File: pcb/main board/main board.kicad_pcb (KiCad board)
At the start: 2 copper layers, 115 x 160.5 mm, 75 parts, among them J1 Motor 0 Conn, J10 12V Battery, J11 BAU, J12 Servo 4 Conn, J13 Servo 1 Conn, J14 Servo 2 Conn, J15 Servo 3 Conn, J16 Servo 5 Conn, J17 Servo 6 Conn, J18 Servo 7 Conn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

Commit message: Added logos and aisler logo placeholder
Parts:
- added G***: LOGO, LOGO, F.Cu at (247.0, 101.0)
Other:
- board text added: "Made by Piment Robotique"

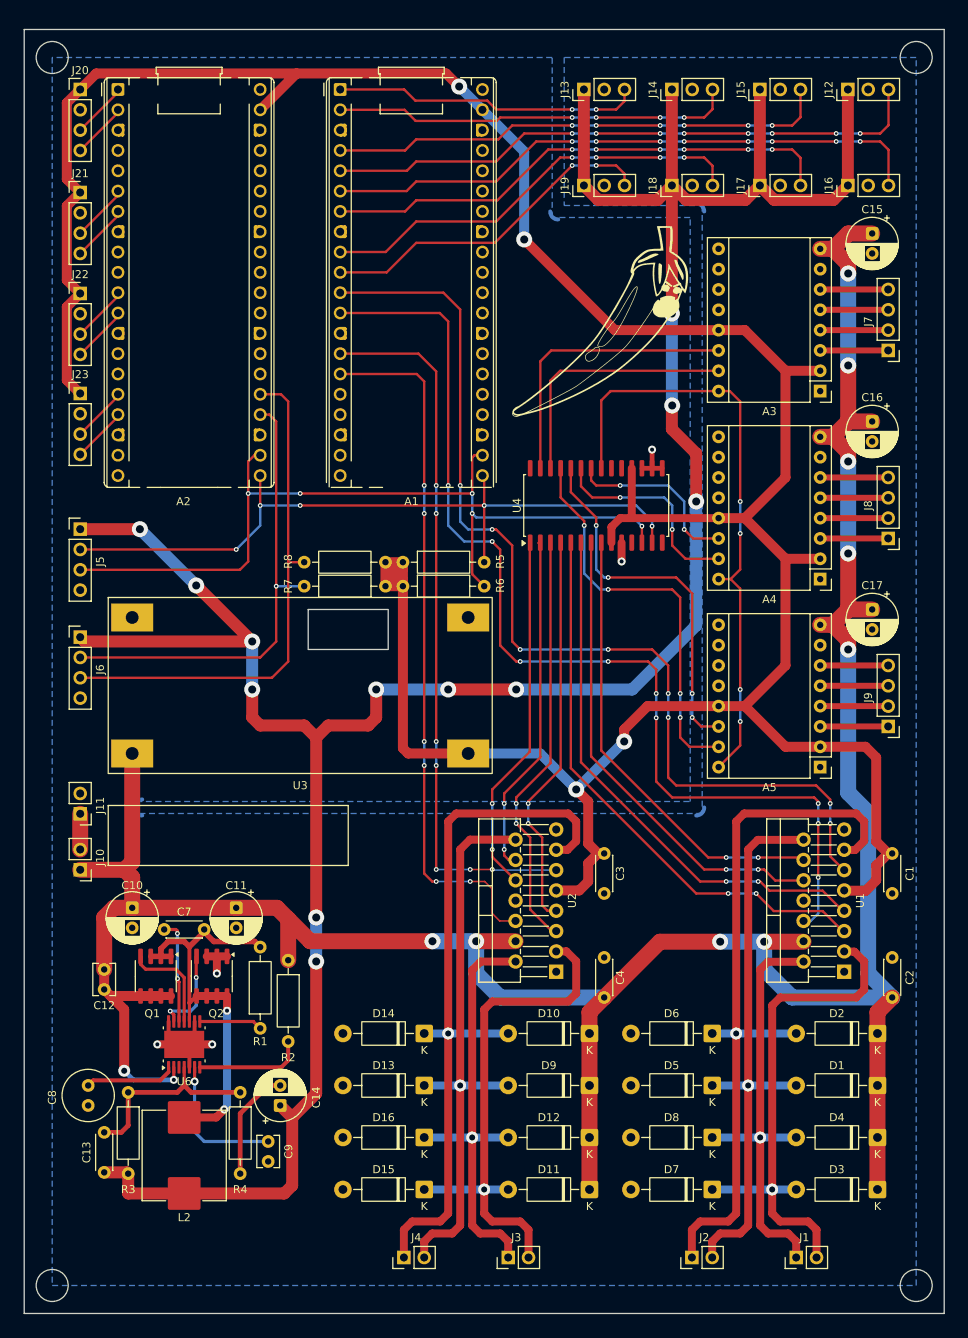
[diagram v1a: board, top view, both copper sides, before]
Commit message: Corrected superposition errors
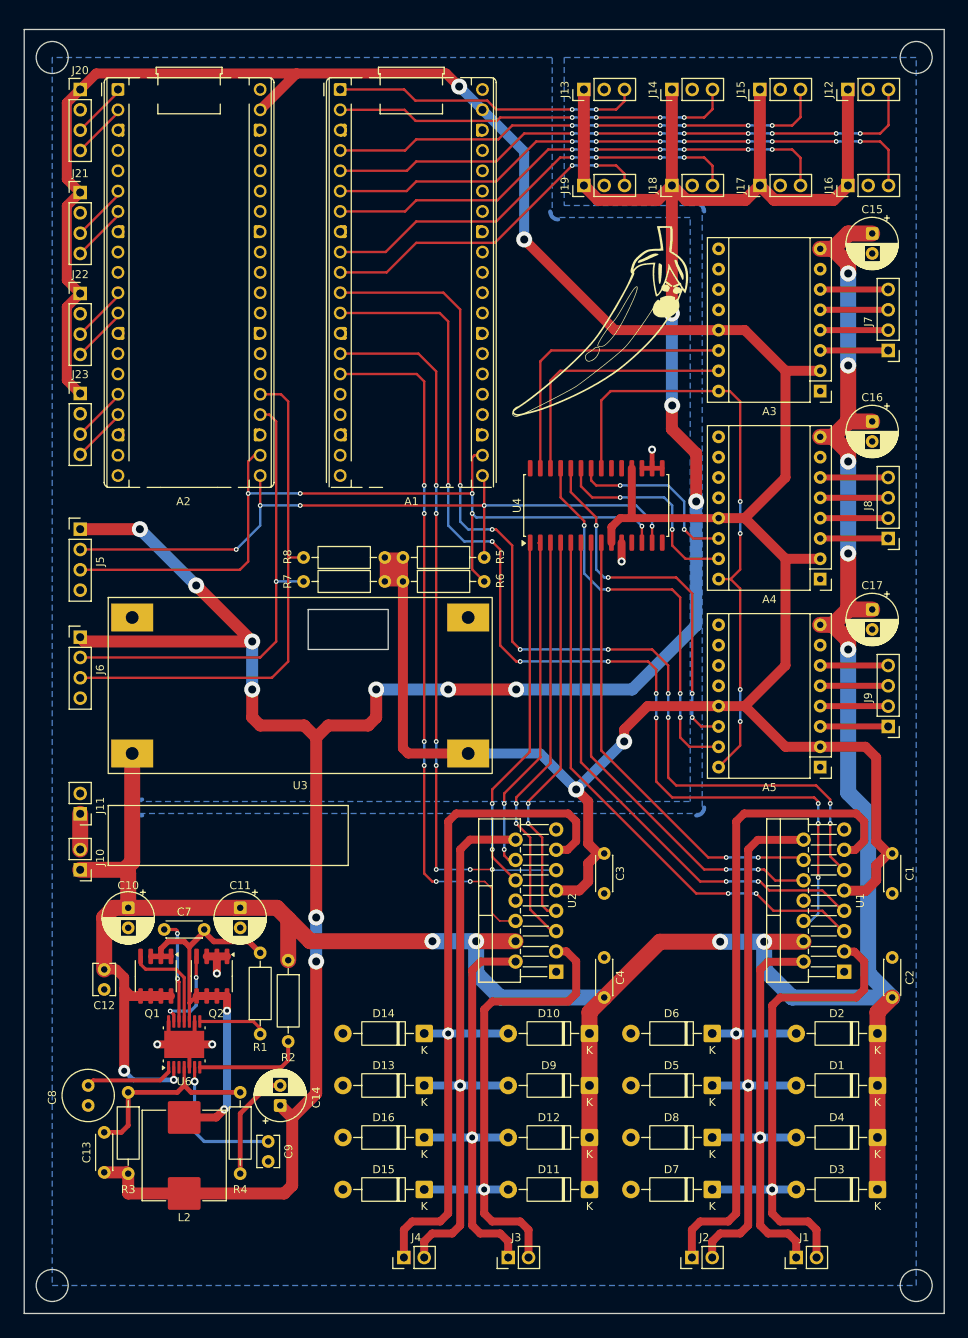
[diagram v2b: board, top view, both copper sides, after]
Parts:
- moved R1 0.72 mm to (204.5, 190.1)
- moved R7 0.60 mm to (220.1, 133.5)
- moved R8 0.60 mm to (220.1, 130.5)
- moved R5 0.59 mm to (222.3, 130.5)
- moved R6 0.59 mm to (222.3, 133.5)
- moved C10 0.50 mm to (188.0, 174.3)
- moved C11 0.50 mm to (202.0, 174.3)
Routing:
- net +5VL: track 389.4 -> 390.2 mm
- net Net-(U6-ILIM): track 7.91 -> 8.62 mm
- net +12V: track 356.2 -> 355.5 mm
- net I2C 0 SDA: track 93.4 -> 92.8 mm
- net I2C 0 SCL: track 105.8 -> 105.2 mm

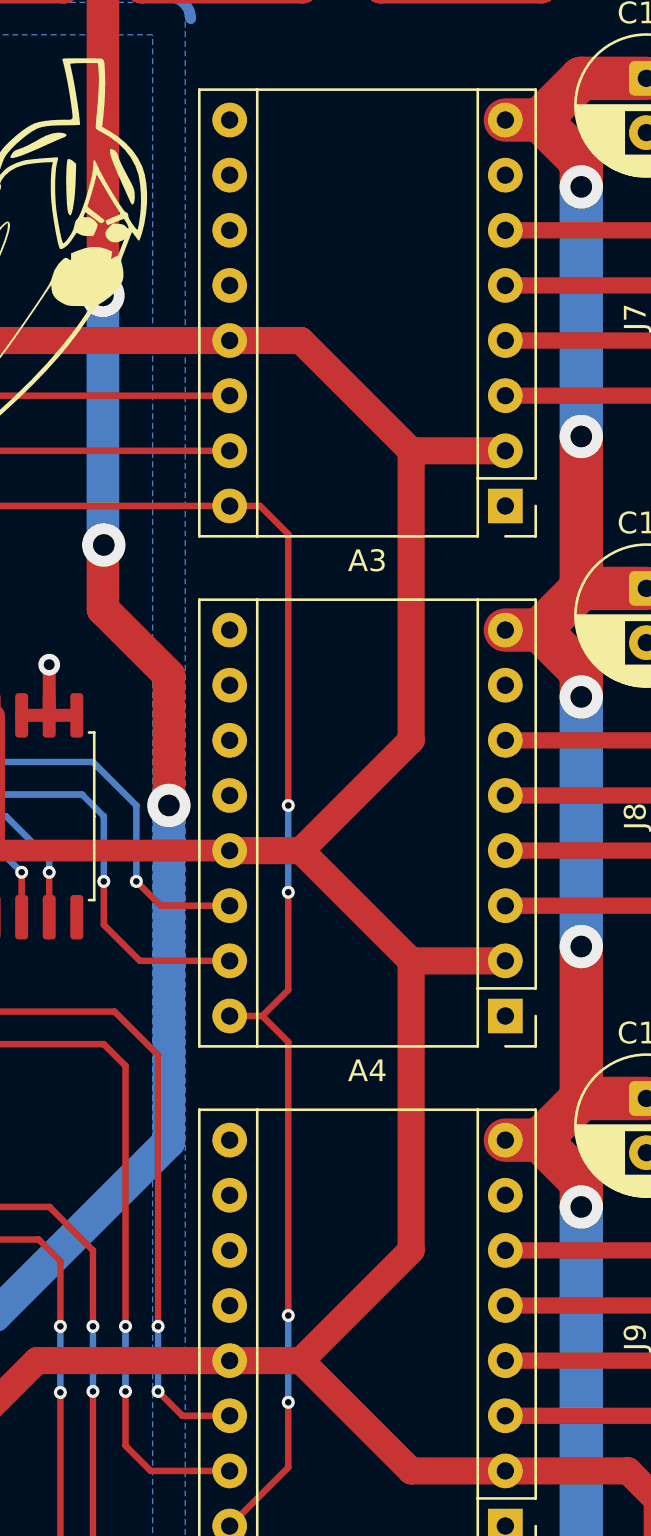
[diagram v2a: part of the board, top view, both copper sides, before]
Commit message: Added Jumpers To select Steppers speed
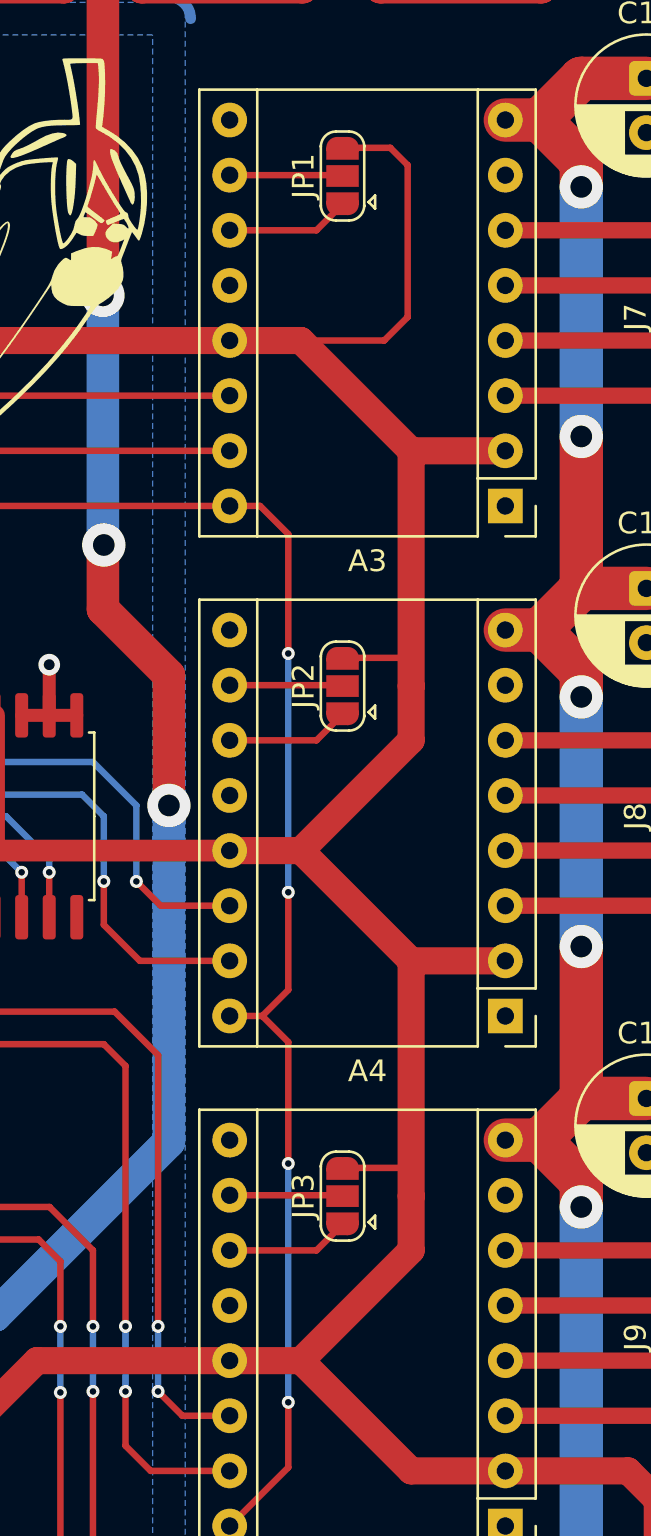
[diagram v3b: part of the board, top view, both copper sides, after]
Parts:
- added JP1: SolderJumper_3_Open, Jumper:SolderJumper-3_P1.3mm_Open_RoundedPad1.0x1.5mm, F.Cu at (267.0, 94.5)
- added JP2: SolderJumper_3_Open, Jumper:SolderJumper-3_P1.3mm_Open_RoundedPad1.0x1.5mm, F.Cu at (267.0, 118.0)
- added JP3: SolderJumper_3_Open, Jumper:SolderJumper-3_P1.3mm_Open_RoundedPad1.0x1.5mm, F.Cu at (267.0, 141.5)
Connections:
- A3 pad 10: unconnected-(A3-MS1-Pad10) -> Net-(A3-MS1)
- A4 pad 10: unconnected-(A4-MS1-Pad10) -> Net-(A4-MS1)
- A5 pad 10: unconnected-(A5-MS1-Pad10) -> Net-(A5-MS1)
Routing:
- net +5VL: track 390.2 -> 412.2 mm
- net GNDPWR: track 29.3 -> 46.4 mm
- net Net-(A5-MS1): track 0.00 -> 5.16 mm
- net Net-(A4-MS1): track 0.00 -> 5.16 mm
- net Net-(A3-MS1): track 0.00 -> 5.16 mm

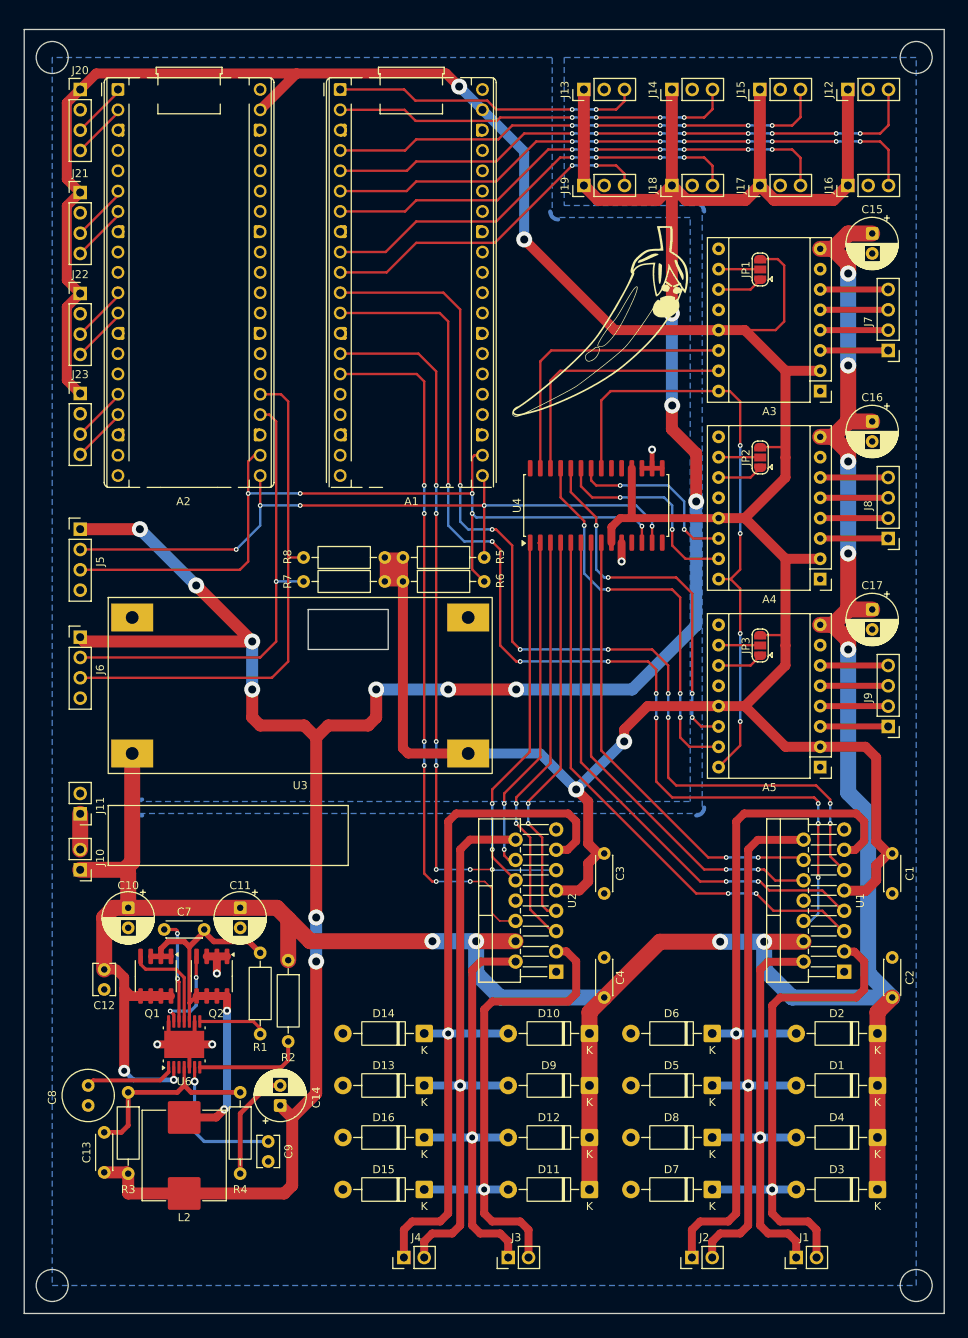
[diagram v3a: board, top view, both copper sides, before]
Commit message: Finished correcting and updating footprints for capacitors and started to change connectors footprints
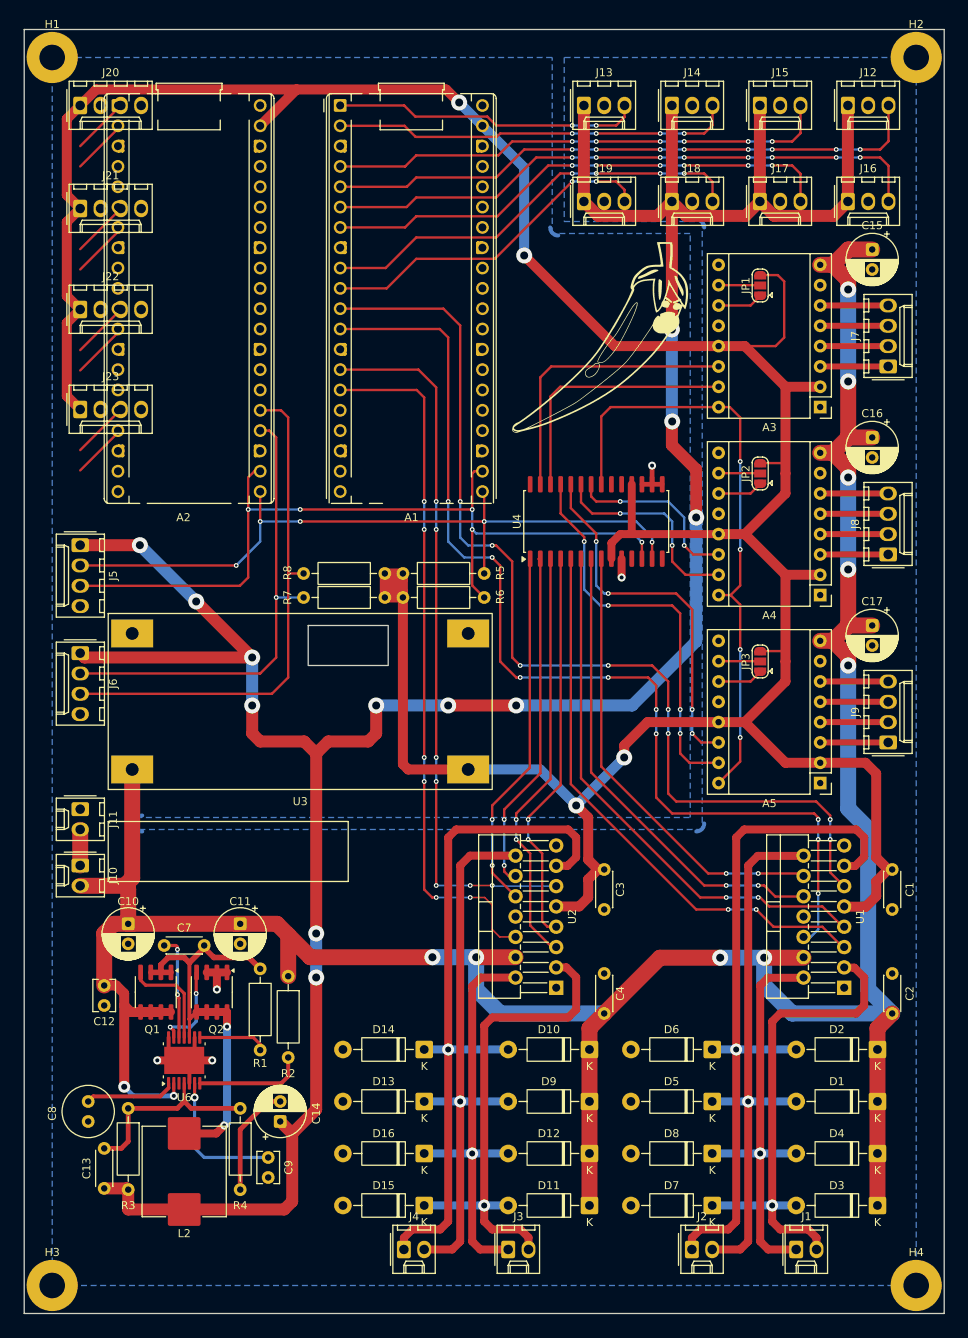
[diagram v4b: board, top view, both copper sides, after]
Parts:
- added H1: MountingHole_Pad, MountingHole:MountingHole_3.2mm_M3_Pad, F.Cu at (178.5, 68.0)
- added H2: MountingHole_Pad, MountingHole:MountingHole_3.2mm_M3_Pad, F.Cu at (286.5, 68.0)
- added H3: MountingHole_Pad, MountingHole:MountingHole_3.2mm_M3_Pad, F.Cu at (178.5, 221.5)
- added H4: MountingHole_Pad, MountingHole:MountingHole_3.2mm_M3_Pad, F.Cu at (286.5, 221.5)
- J1, J10, J11, J2, J3, J4: footprint Connector_PinHeader_2.54mm:PinHeader_1x02_P2.54mm_Vertical -> Connector_Molex:Molex_KK-254_AE-6410-02A_1x02_P2.54mm_Vertical
- J12, J13, J14, J15, J16, J17, J18, J19: footprint Connector_PinHeader_2.54mm:PinHeader_1x03_P2.54mm_Vertical -> Connector_Molex:Molex_KK-254_AE-6410-03A_1x03_P2.54mm_Vertical
- J20, J21, J22, J23, J5, J6, J7, J8, J9: footprint Connector_PinHeader_2.54mm:PinHeader_1x04_P2.54mm_Vertical -> Connector_Molex:Molex_KK-254_AE-6410-04A_1x04_P2.54mm_Vertical
- moved J5 2.00 mm to (182.0, 129.0), turned to -90 degrees
- moved A1 2.00 mm to (214.5, 74.0)
- moved A2 2.00 mm to (186.7, 74.0)
- moved A3 2.00 mm to (274.5, 111.7)
- moved A4 2.00 mm to (274.5, 135.2)
- moved A5 2.00 mm to (274.5, 158.7)
- moved C1 2.00 mm to (283.5, 169.5)
- moved C10 2.00 mm to (188.0, 176.3)
- moved C11 2.00 mm to (202.0, 176.3)
- moved C12 2.00 mm to (185.0, 184.0)
- moved C13 2.00 mm to (185.0, 209.4)
- moved C14 2.00 mm to (207.0, 201.0)
- moved C15 2.00 mm to (281.0, 92.0)
- moved C16 2.00 mm to (281.0, 115.5)
- moved C17 2.00 mm to (281.0, 139.0)
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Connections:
- J10 pad 1: +12V -> Net-(J10-Pin_1)
- J10 pad 2: Net-(J10-Pin_2) -> +12V
- J11 pad 1: Net-(J10-Pin_2) -> GNDPWR
- J11 pad 2: GNDPWR -> Net-(J10-Pin_1)
- J12 pad 1: +5VP -> Servo 4 PWM
- J12 pad 3: Servo 4 PWM -> +5VP
- J13 pad 1: +5VP -> Servo 1 PWM
- J13 pad 3: Servo 1 PWM -> +5VP
- J14 pad 1: +5VP -> Servo 2 PWM
- J14 pad 3: Servo 2 PWM -> +5VP
- J15 pad 1: +5VP -> Servo 3 PWM
- J15 pad 3: Servo 3 PWM -> +5VP
- J16 pad 1: +5VP -> Servo 5 PWM
- J16 pad 3: Servo 5 PWM -> +5VP
- J17 pad 1: +5VP -> Servo 6 PWM
- J17 pad 3: Servo 6 PWM -> +5VP
- J18 pad 1: +5VP -> Servo 7 PWM
- J18 pad 3: Servo 7 PWM -> +5VP
- J19 pad 1: +5VP -> Servo 8 PWM
- J19 pad 3: Servo 8 PWM -> +5VP
- J5 pad 1: +5VP -> +5VL
- J6 pad 1: +5VP -> +5VL
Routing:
- net Net-(J10-Pin_2): track 4.46 -> 0.00 mm
- net Net-(J10-Pin_1): track 0.00 -> 4.46 mm
- net Net-(D3-A): track 65.3 -> 62.3 mm
- net Net-(D2-A): track 91.7 -> 88.7 mm
- net Net-(D10-A): track 91.6 -> 88.6 mm
- net Net-(D11-A): track 65.2 -> 62.2 mm
- net Net-(D12-A): track 55.6 -> 53.2 mm
- net Net-(D4-A): track 55.6 -> 53.2 mm
- net Net-(D13-K): track 72.3 -> 69.8 mm
- net Net-(D1-A): track 72.1 -> 69.7 mm
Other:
- outline, holes or cut-outs redrawn
